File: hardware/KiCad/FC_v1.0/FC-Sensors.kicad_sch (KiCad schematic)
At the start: 12 parts, among them U4 ICM-42688-P, U5 MMC5983MA, U6 BMP390

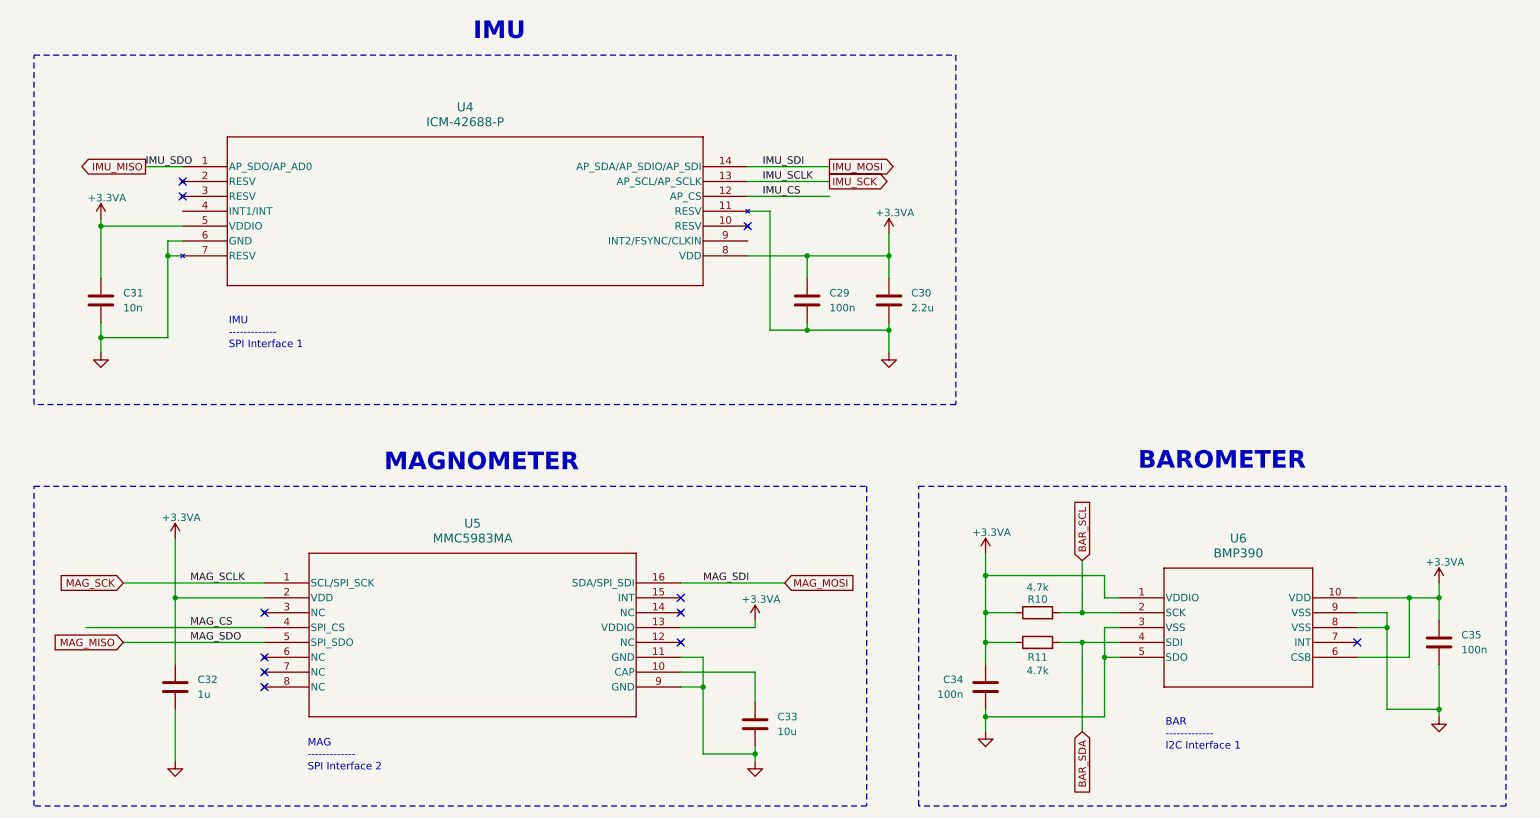
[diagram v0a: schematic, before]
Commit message: ESC PWM Generation
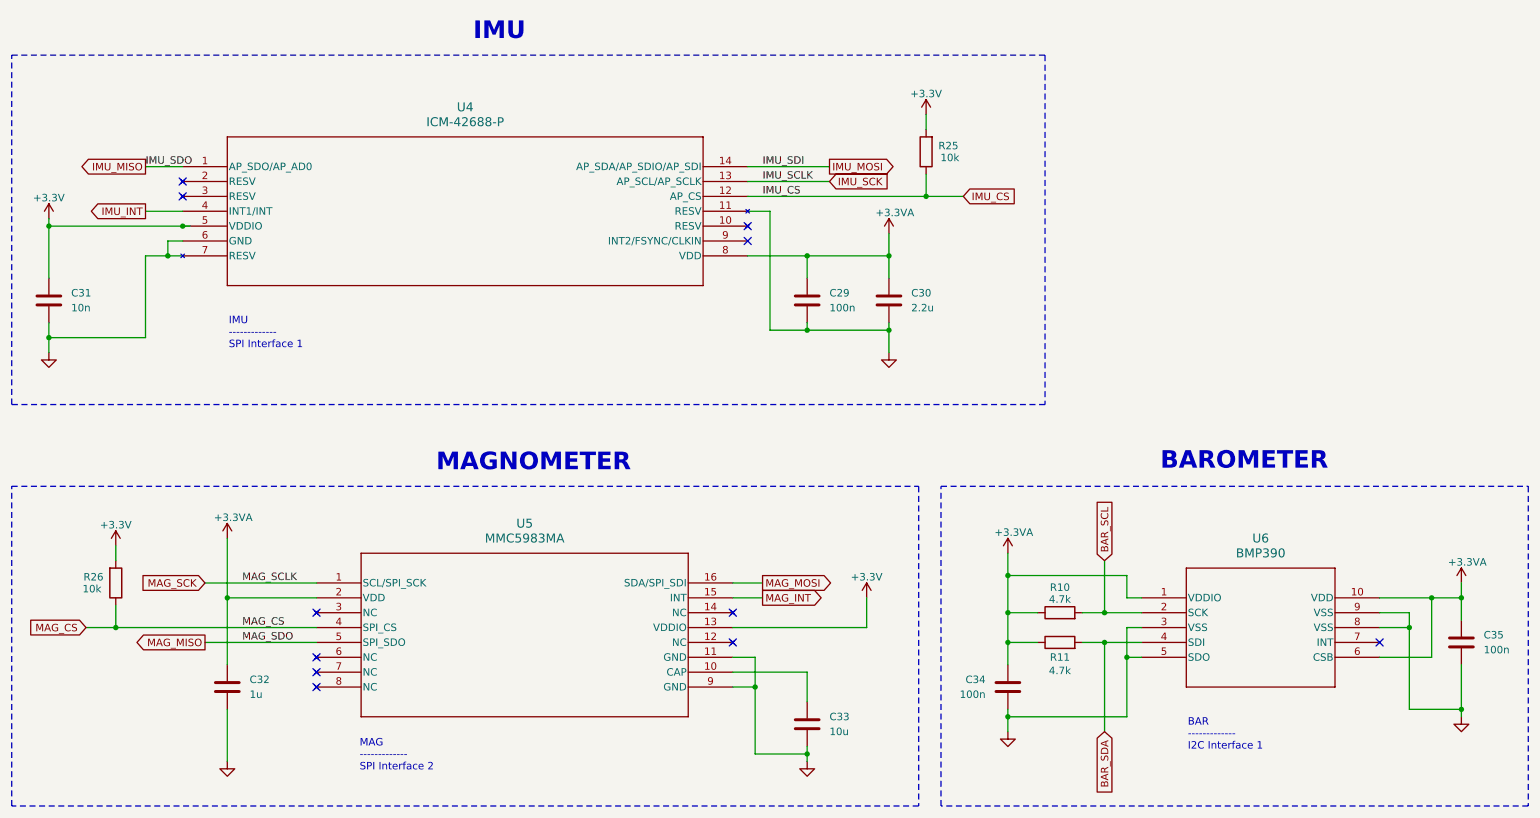
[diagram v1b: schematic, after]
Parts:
- added R25, R26: 10k, symbol Device:R
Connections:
- net +3.3VA: no longer C31.1, U4.5 (VDDIO), U5.13 (VDDIO)
- net IMU_CS: now also R25.1
- net MAG_CS: now also R26.1
- net IMU_INT: now reaches U4.4 (INT1/INT)
- net MAG_INT: now reaches U5.15 (INT)
- new net +3.3V: C31.1, R25.2, R26.2, U4.5 (VDDIO), U5.13 (VDDIO)
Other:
- moved on the sheet: C31, C32, C33, C34, C35, R10, R11, U5, U6
